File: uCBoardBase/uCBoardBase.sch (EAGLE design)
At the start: 21 parts, among them U1 TM4C123BE6PMSMD, U2 TPS73633DBVR, Y1 16 MHz

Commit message: Updated Schematic
Updated schematic
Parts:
- removed FRAME1: FRAME-LETTER, SparkFun-Aesthetics:FRAME-LETTER
- added C14, C15: 10pF, SparkFun-Passives:CAP0603-CAP
- added C16, C17: 0.1uF, SparkFun-Passives:CAP0603-CAP
- added C18: 10uF, SparkFun-Passives:CAP_POL1206-KIT
- added C19, C20: 47pF, SparkFun-Passives:CAP0603-CAP
- added F1: PTCSMD, SparkFun-PowerIC:PTCSMD
- added JP2: USBSMD, SparkFun-Connectors:USBSMD
- added LED2, LED3: (no value), SparkFun-LED:LED0603
- added R3: 0, SparkFun-Passives:RESISTOR0603-RES
- added R4, R5: 270, SparkFun-Passives:RESISTOR0603-RES
- added R6, R7: 27, SparkFun-Passives:RESISTOR0603-RES
- added STANDOFF1, STANDOFF2, STANDOFF3, STANDOFF4: STAND-OFF, SparkFun-Electromechanical:STAND-OFF
- added U3: ARDUINO_SHIELDNO_SILK, SparkFun-Boards:ARDUINO_SHIELDNO_SILK
- added U4: FT230XSSOP, SparkFun-DigitalIC:FT230XSSOP
- added Y2: 32.768 kHz, SparkFun-FreqCtrl:CRYSTALTC26H
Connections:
- new net !HIB: U1A.!HIB
- new net !WAKE: U1A.!WAKE
- new net 5V: C16.1, C18.+, F1.2, R4.2, R5.2, U4.VCC
- new net GND: C16.2, C17.2, C18.-, C19.2, C20.2, JP2.GND, U4.GND@13, U4.GND@5
- new net N$10: C15.1, U1A.XOSC0, Y2.2
- new net N$11: C14.2, C15.2, U1A.GNDX
- new net N$12: LED3.A, R5.1
- new net N$13: LED2.A, R4.1
- new net N$14: F1.1, JP2.VBUS
- new net N$15: R7.1, U4.USBDP
- new net N$16: R6.1, U4.USBDM
- new net N$17: C17.1, U4.!RESET, U4.3V3OUT, U4.VCCIO
- new net N$4: C19.1, JP2.D-, R6.2
- new net N$7: C20.1, JP2.D+, R7.2
- new net N$9: C14.1, U1A.XOSC1, Y2.1
- new net RXD: U4.RXD
- new net RXLED: LED2.C, U4.CBUS1
- new net TXD: U4.TXD
- new net TXLED: LED3.C, U4.CBUS2
- new net VBAT: R3.2, U1A.VBAT
- net 3.3V: now also R3.1
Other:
- moved on the sheet: C11, C12, C13, R1, S1, Y1

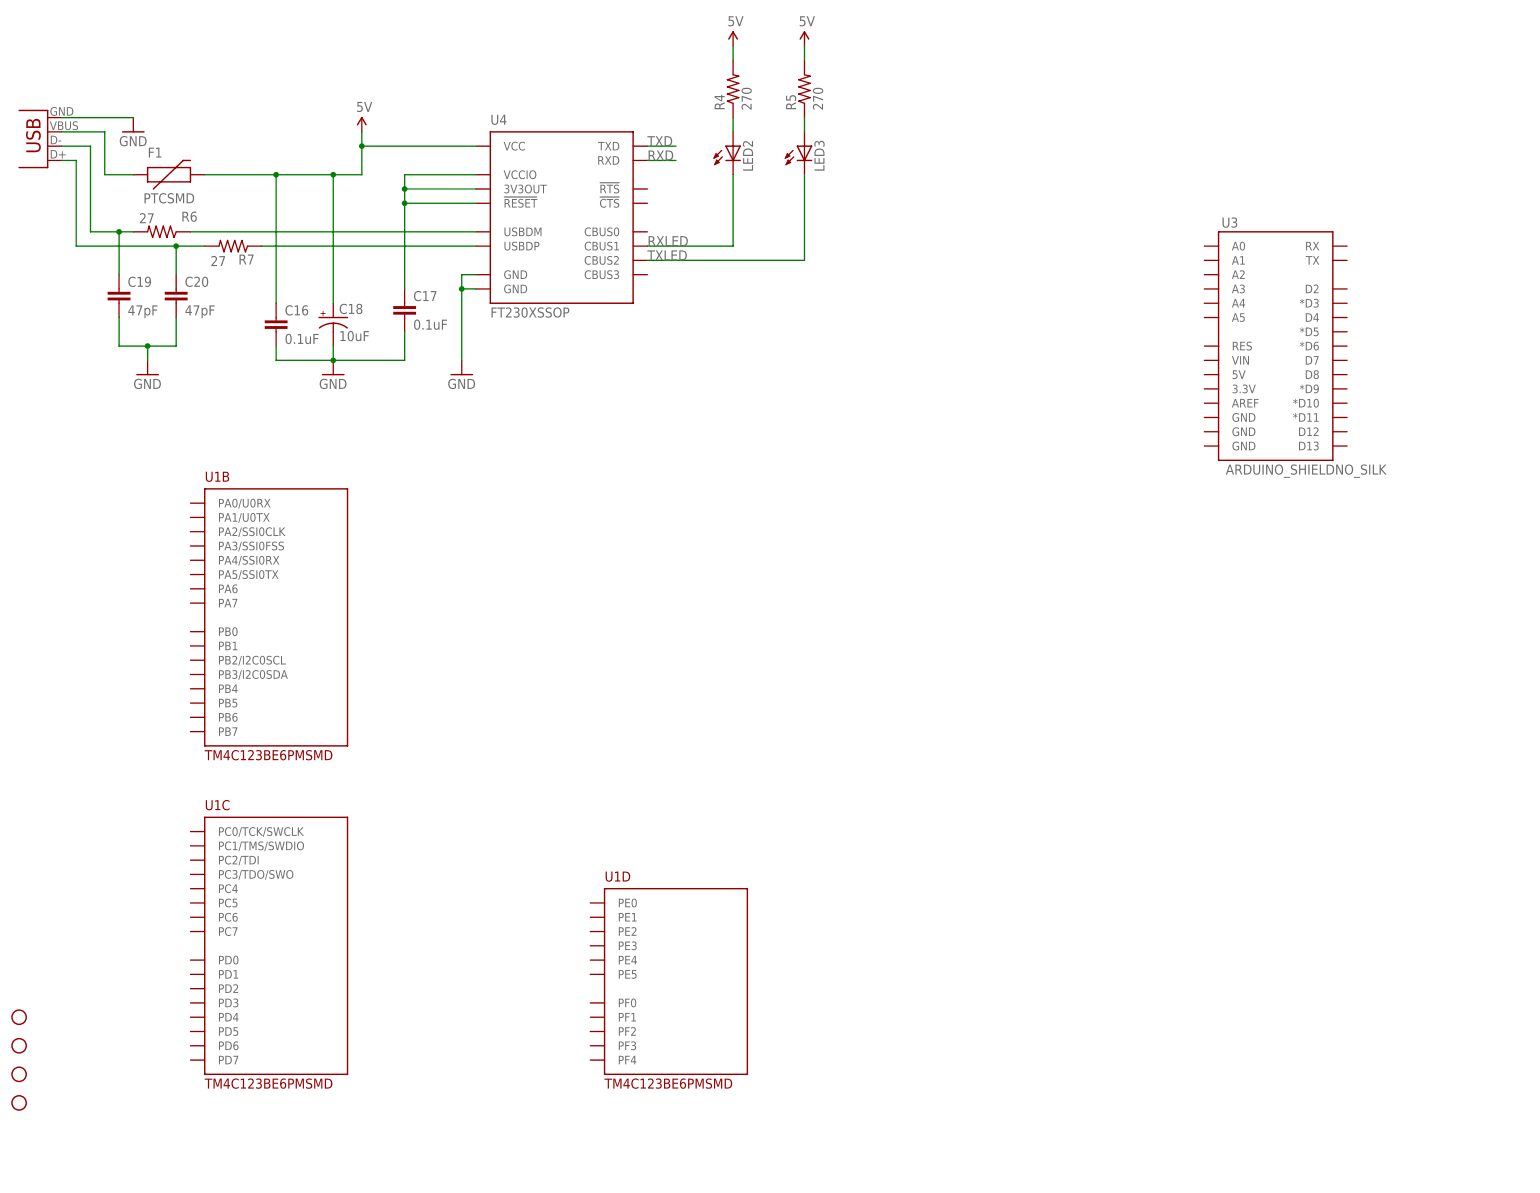
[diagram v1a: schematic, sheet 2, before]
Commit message: Updated Schematic and Layout
Updated schematic and finished board layout
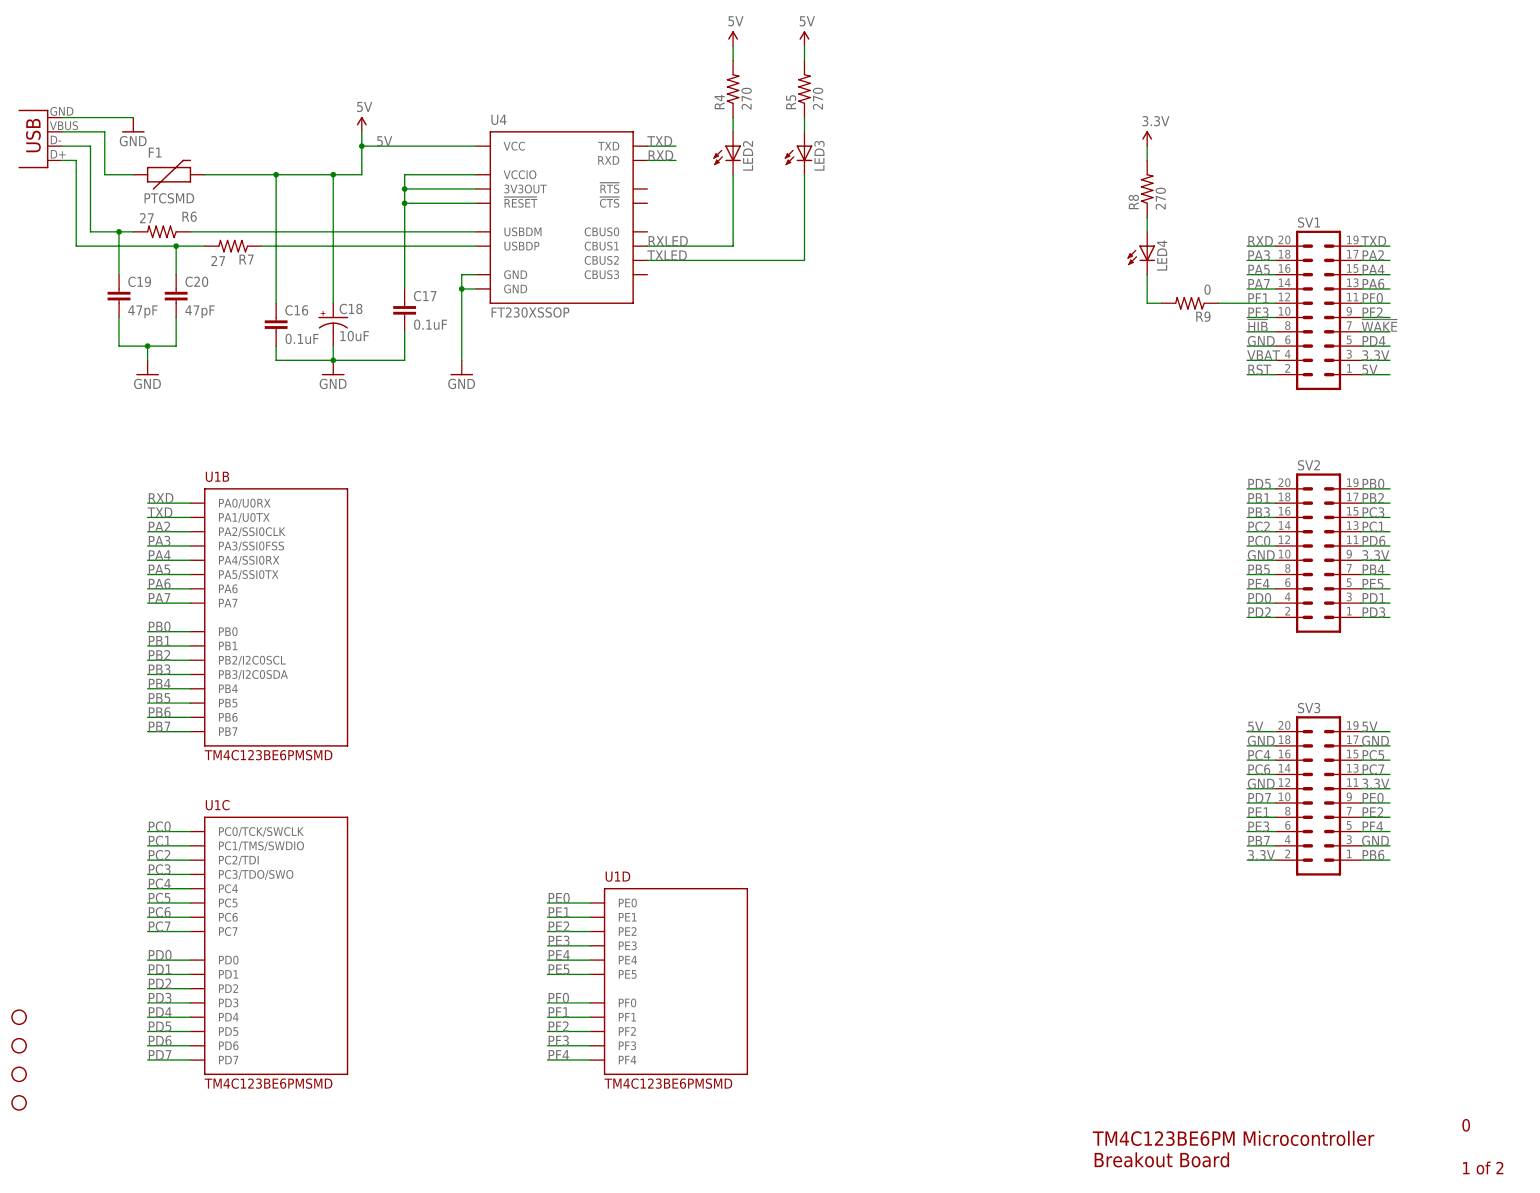
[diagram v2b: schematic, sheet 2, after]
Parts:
- removed U3: ARDUINO_SHIELDNO_SILK, SparkFun-Boards:ARDUINO_SHIELDNO_SILK
- added J1: POWER_JACKPTH, SparkFun-Connectors:POWER_JACKPTH
- added LED4: (no value), SparkFun-LED:LED0603
- added R8: 270, SparkFun-Passives:RESISTOR0603-RES
- added R9: 0, SparkFun-Passives:RESISTOR0603-RES
- added SV1, SV2, SV3: (no value), con-lstb:MA10-2
- S1: value SWITCH-MOMENTARY-2-SMD-1101NE -> Switch
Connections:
- removed net N$5: C9.1, U2.IN
- new net PA2: SV1.17, U1B.PA2/SSI0CLK
- new net PA3: SV1.18, U1B.PA3/SSI0FSS
- new net PA4: SV1.15, U1B.PA4/SSI0RX
- new net PA5: SV1.16, U1B.PA5/SSI0TX
- new net PA6: SV1.13, U1B.PA6
- new net PA7: SV1.14, U1B.PA7
- new net PB0: SV2.19, U1B.PB0
- new net PB1: SV2.18, U1B.PB1
- new net PB2: SV2.17, U1B.PB2/I2C0SCL
- new net PB3: SV2.16, U1B.PB3/I2C0SDA
- new net PB4: SV2.7, U1B.PB4
- new net PB5: SV2.8, U1B.PB5
- new net PB6: SV3.1, U1B.PB6
- new net PB7: SV3.4, U1B.PB7
- new net PC0: SV2.12, U1C.PC0/TCK/SWCLK
- new net PC1: SV2.13, U1C.PC1/TMS/SWDIO
- new net PC2: SV2.14, U1C.PC2/TDI
- new net PC3: SV2.15, U1C.PC3/TDO/SWO
- new net PC4: SV3.16, U1C.PC4
- new net PC5: SV3.15, U1C.PC5
- new net PC6: SV3.14, U1C.PC6
- new net PC7: SV3.13, U1C.PC7
- new net PD0: SV2.4, U1C.PD0
- new net PD1: SV2.3, U1C.PD1
- new net PD2: SV2.2, U1C.PD2
- new net PD3: SV2.1, U1C.PD3
- new net PD4: SV1.5, U1C.PD4
- new net PD5: SV2.20, U1C.PD5
- new net PD6: SV2.11, U1C.PD6
- new net PD7: SV3.10, U1C.PD7
- new net PE0: SV3.9, U1D.PE0
- new net PE1: SV3.8, U1D.PE1
- new net PE2: SV3.7, U1D.PE2
- new net PE3: SV3.6, U1D.PE3
- new net PE4: SV2.6, U1D.PE4
- new net PE5: SV2.5, U1D.PE5
- new net PF0: SV1.11, U1D.PF0
- new net PF1: R9.1, SV1.12, U1D.PF1
- new net PF2: SV1.9, U1D.PF2
- new net PF3: SV1.10, U1D.PF3
- new net PF4: SV3.5, U1D.PF4
- new net RST: C11.1, R1.1, S1.1, SV1.2, U1A.!RST
- new net TXLED1: LED4.C, R9.2
- net !HIB: now also SV1.8
- net !WAKE: now also SV1.7
- net 3.3V: now also R8.2, SV1.3, SV2.9, SV3.11, SV3.2; no longer C1.2, C10.2, C11.2, C12.2, C13.2, C2.2, C3.2, C4.2, C5.2, C6.2, C7.2, C8.2, C9.2, LED1.C, S1.2, U1A.GND@12, U1A.GND@27, U1A.GND@39, U1A.GND@55, U1A.GNDA, U2.GND
- net 5V: now also C9.1, J1.PWR, SV1.1, SV3.19, SV3.20, U2.IN
- net GND: now also C1.2, C10.2, C11.2, C12.2, C13.2, C2.2, C3.2, C4.2, C5.2, C6.2, C7.2, C8.2, C9.2, J1.GND, J1.GNDBREAK, LED1.C, S1.2, SV1.6, SV2.10, SV3.12, SV3.17, SV3.18, SV3.3, U1A.GND@12, U1A.GND@27, U1A.GND@39, U1A.GND@55, U1A.GNDA, U2.GND
- net N$1: now also LED4.A, R8.1; no longer C11.1, R1.1, S1.1, U1A.!RST
- net RXD: now also SV1.20, U1B.PA0/U0RX
- net TXD: now also SV1.19, U1B.PA1/U0TX
- net VBAT: now also SV1.4
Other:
- note added: "0"
- note added: "1 of 2"
- note added: "TM4C123BE6PM Microcontroller Breakout Board"
- moved on the sheet: C1, C9, LED1, R2, R3, U2

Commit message: Updated README
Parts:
- added CC_TEXT1, CC_TEXT2: CREATIVE_COMMONS, SparkFun-Aesthetics:CREATIVE_COMMONS
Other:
- note added: "B. Carrizales"
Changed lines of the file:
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@@
 <part name="R9" library="SparkFun-Passives" deviceset="RESISTOR" device="0603-RES" value="0"/>
 <part name="SUPPLY9" library="SparkFun-Aesthetics" deviceset="3.3V" device=""/>
+<part name="CC_TEXT1" library="SparkFun-Aesthetics" deviceset="CREATIVE_COMMONS" device=""/>
+<part name="CC_TEXT2" library="SparkFun-Aesthetics" deviceset="CREATIVE_COMMONS" device=""/>
 </parts>
 <sheets>
@@
 <text x="182.88" y="-114.3" size="2.1844" layer="94">0</text>
 <text x="182.88" y="-121.92" size="2.1844" layer="94">1 of 2</text>
+<text x="22.86" y="-119.38" size="1.778" layer="91">B. Carrizales</text>
 </plain>
 <instances>
@@
 <instance part="GND8" gate="1" x="-30.48" y="-68.58"/>
 <instance part="J1" gate="G$1" x="-53.34" y="-53.34"/>
+<instance part="CC_TEXT1" gate="G$1" x="10.16" y="-119.38"/>
 </instances>
 <busses>
@@
 <text x="61.468" y="-105.41" size="2.54" layer="94">TM4C123BE6PM Microcontroller
 Breakout Board</text>
+<text x="-22.86" y="-104.14" size="1.778" layer="91">B. Carrizales</text>
 </plain>
 <instances>
@@
 <instance part="R9" gate="G$1" x="78.74" y="48.26" rot="R180"/>
 <instance part="SUPPLY9" gate="G$1" x="71.12" y="76.2"/>
+<instance part="CC_TEXT2" gate="G$1" x="-35.56" y="-104.14"/>
 </instances>
 <busses>
